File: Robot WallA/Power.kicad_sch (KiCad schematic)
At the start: 25 parts, among them IC6 TLV75533PDBVR, J10 Conn_01x02, J11 Conn_01x02, J12 Conn_01x02, J7 Conn_01x02, J8 XT90PW_M, J9 Conn_01x02

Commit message: Continue to route
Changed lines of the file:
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@@
+	)
+	(label "5V_ACTUATORS"
+		(at 257.81 153.67 180)
+		(effects
+			(font
+				(size 1.27 1.27)
+			)
+			(justify right bottom)
+		)
 	)
 	(label "5V_ACTUATORS"
@@
 		)
 	)
+	(label "12V"
+		(at 257.81 146.05 180)
+		(effects
+			(font
+				(size 1.27 1.27)
+			)
+			(justify right bottom)
+		)
+	)
 	(label "Vbatt"
 		(at 41.91 99.06 0)
@@
 		)
 	)
+	(label "5V_COMPUTE"
+		(at 257.81 149.86 180)
+		(effects
+			(font
+				(size 1.27 1.27)
+			)
+			(justify right bottom)
+		)
+	)
 	(label "5V_ACTUATORS"
 		(at 257.81 128.27 180)
@@
 	(label "3V3"
 		(at 130.81 76.2 180)
+		(effects
+			(font
+				(size 1.27 1.27)
+			)
+			(justify right bottom)
+		)
+	)
+	(label "24V"
+		(at 257.81 142.24 180)
 		(effects
 			(font
@@
 			)
 			(justify left)
+		)
+	)
+	(netclass_flag ""
+		(length 2.54)
+		(shape round)
+		(at 257.81 153.67 270)
+		(effects
+			(font
+				(size 1.27 1.27)
+			)
+			(justify right bottom)
+		)
+		(property "Netclass" "HighCurrent_3A"
+			(at 261.112 153.67 0)
+			(effects
+				(font
+					(size 1.27 1.27)
+				)
+				(justify left)
+			)
+		)
+		(property "Component Class" ""
+			(at -34.29 92.71 0)
+			(effects
+				(font
+					(size 1.27 1.27)
+					(italic yes)
+				)
+			)
+		)
+	)
+	(netclass_flag ""
+		(length 2.54)
+		(shape round)
+		(at 257.81 142.24 270)
+		(effects
+			(font
+				(size 1.27 1.27)
+			)
+			(justify right bottom)
+		)
+		(property "Netclass" "HighCurrent_5A"
+			(at 261.112 142.24 0)
+			(effects
+				(font
+					(size 1.27 1.27)
+				)
+				(justify left)
+			)
+		)
+		(property "Component Class" ""
+			(at -34.29 81.28 0)
+			(effects
+				(font
+					(size 1.27 1.27)
+					(italic yes)
+				)
+			)
+		)
+	)
+	(netclass_flag ""
+		(length 2.54)
+		(shape round)
+		(at 257.81 149.86 270)
+		(effects
+			(font
+				(size 1.27 1.27)
+			)
+			(justify right bottom)
+		)
+		(property "Netclass" "HighCurrent_3A"
+			(at 261.112 149.86 0)
+			(effects
+				(font
+					(size 1.27 1.27)
+				)
+				(justify left)
+			)
+		)
+		(property "Component Class" ""
+			(at -34.29 88.9 0)
+			(effects
+				(font
+					(size 1.27 1.27)
+					(italic yes)
+				)
+			)
+		)
+	)
+	(netclass_flag ""
+		(length 2.54)
+		(shape round)
+		(at 36.83 99.06 180)
+		(effects
+			(font
+				(size 1.27 1.27)
+			)
+			(justify right bottom)
+		)
+		(property "Netclass" "HighCurrent_5A"
+			(at 43.18 103.378 0)
+			(effects
+				(font
+					(size 1.27 1.27)
+				)
+				(justify right)
+			)
+		)
+		(property "Component Class" ""
+			(at 97.79 -193.04 90)
+			(effects
+				(font
+					(size 1.27 1.27)
+					(italic yes)
+				)
+			)
+		)
+	)
+	(netclass_flag ""
+		(length 2.54)
+		(shape round)
+		(at 257.81 146.05 270)
+		(effects
+			(font
+				(size 1.27 1.27)
+			)
+			(justify right bottom)
+		)
+		(property "Netclass" "HighCurrent_5A"
+			(at 261.112 146.05 0)
+			(effects
+				(font
+					(size 1.27 1.27)
+				)
+				(justify left)
+			)
+		)
+		(property "Component Class" ""
+			(at -34.29 85.09 0)
+			(effects
+				(font
+					(size 1.27 1.27)
+					(italic yes)
+				)
+			)
 		)
 	)
@@
 		(on_board yes)
 		(dnp no)
-		(fields_autoplaced yes)
 		(property "Reference" "#PWR049"
 			(at 34.29 100.33 0)
@@
 		)
 		(property "Value" "GND"
-			(at 34.29 99.06 0)
-			(effects
-				(font
+			(at 34.036 97.79 0)
+			(effects
+				(font

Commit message: Updated fab files.
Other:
- company: (none) -> Socotec Monitoring
- title: (none) -> Robot Wall-A
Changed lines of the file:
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@@
 	(generator_version "9.0")
 	(paper "A4")
+	(title_block
+		(title "Robot Wall-A")
+		(date "2025-09-20")
+		(rev "v1.0")
+		(company "Socotec Monitoring")
+		(comment 1 "GDU")
+		(comment 2 "THO")
+	)
 	(text "Cavaliers spécial qui résistent à 5A"
 		(exclude_from_sim no)
@@
 			)
 		)
+		(property "MPN" ""
+			(at 257.81 120.65 90)
+			(effects
+				(font
+					(size 1.27 1.27)
+				)
+				(hide yes)
+			)
+		)
 		(pin "1"
 		)
@@
 			)
 		)
+		(property "MPN" ""
+			(at 118.11 133.35 90)
+			(effects
+				(font
+					(size 1.27 1.27)
+				)
+				(hide yes)
+			)
+		)
 		(pin "1"
 		)
@@
 			)
 		)
+		(property "MPN" ""
+			(at 34.29 88.9 90)
+			(effects
+				(font
+					(size 1.27 1.27)
+				)
+				(hide yes)
+			)
+		)
 		(pin "1"
 		)
@@
 			)
 		)
+		(property "MPN" ""
+			(at 77.47 162.56 0)
+			(effects
+				(font
+					(size 1.27 1.27)
+				)
+				(hide yes)
+			)
+		)
 		(pin "1"
 		)
@@
 			)
 		)
+		(property "MPN" ""
+			(at 257.81 116.84 90)
+			(effects
+				(font
+					(size 1.27 1.27)
+				)
+				(hide yes)
+			)
+		)
 		(pin "1"
 		)
@@
 			)
 		)
+		(property "MPN" ""
+			(at 77.47 172.72 0)
+			(effects
+				(font
+					(size 1.27 1.27)
+				)
+				(hide yes)
+			)
+		)
 		(pin "1"
 		)
@@
 			)
 		)
+		(property "MPN" ""
+			(at 36.83 137.16 0)
+			(effects
+				(font
+					(size 1.27 1.27)
+				)
+				(hide yes)
+			)
+		)
 		(instances
 			(project "Robot WallA"
@@
 			)
 		)
+		(property "MPN" ""
+			(at 262.89 88.9 0)
+			(effects
+				(font
+					(size 1.27 1.27)
+				)
+				(hide yes)
+			)
+		)
 		(pin "1"
 		)
@@
 			)
 		)
+		(property "MPN" ""
+			(at 36.83 128.27 0)
+			(effects
+				(font
+					(size 1.27 1.27)
+				)
+				(hide yes)
+			)
+		)
 		(instances
 			(project "Robot WallA"
@@
 			)
 		)
+		(property "MPN" ""
+			(at 262.89 96.52 0)
+			(effects
+				(font
+					(size 1.27 1.27)
+				)
+				(hide yes)
+			)
+		)
 		(pin "1"
 		)
@@
 			)
 		)
+		(property "MPN" ""
+			(at 127 31.75 90)
+			(effects
+				(font
+					(size 1.27 1.27)
+				)
+				(hide yes)
+			)
+		)
 		(pin "2"
 		)
@@
 			)
 		)
+		(property "MPN" ""
+			(at 116.84 74.93 90)
+			(effects
+				(font
+					(size 1.27 1.27)
+				)
+				(hide yes)
+			)
+		)
 		(pin "1"
 		)
@@
 			)
 		)
+		(property "MPN" ""
+			(at 160.02 179.07 0)
+			(effects
+				(font
+					(size 1.27 1.27)
+				)
+				(hide yes)
+			)
+		)
 		(pin "1"
 		)
@@
 			)
 		)
+		(property "MPN" ""
+			(at 257.81 132.08 90)
+			(effects
+				(font
+					(size 1.27 1.27)
+				)
+				(hide yes)
+			)
+		)
 		(pin "1"
 		)
@@
 			)
 		)
+		(property "MPN" ""
+			(at 118.11 172.72 0)
+			(effects
+				(font
+					(size 1.27 1.27)
+				)
+				(hide yes)
+			)
+		)
 		(pin "5"
 		)
@@
 			)
 		)
+		(property "MPN" ""
+			(at 123.19 109.22 90)
+			(effects
+				(font
+					(size 1.27 1.27)
+				)
+				(hide yes)
+			)
+		)
 		(pin "2"
 		)
@@
 			)
 		)
+		(property "MPN" ""
+			(at 257.81 124.46 90)
+			(effects
+				(font
+					(size 1.27 1.27)
+				)
+				(hide yes)
+			)
+		)
 		(pin "1"
 		)
@@
 			)
 		)
+		(property "MPN" ""
+			(at 148.59 179.07 0)
+			(effects
+				(font
+					(size 1.27 1.27)
+				)
+				(hide yes)
+			)
+		)
 		(pin "1"
 		)
@@
 			)
 		)
+		(property "MPN" ""
+			(at 116.84 104.14 90)
+			(effects
+				(font
+					(size 1.27 1.27)
+				)
+				(hide yes)
+			)
+		)
 		(pin "1"
 		)
@@
 			)
 		)
+		(property "MPN" ""
+			(at 102.87 176.53 0)
+			(effects
+				(font
+					(size 1.27 1.27)
+				)
+				(hide yes)
+			)
+		)
 		(pin "1"
 		)
@@
 			)
 		)
+		(property "MPN" ""
+			(at 257.81 128.27 90)
+			(effects
+				(font
+					(size 1.27 1.27)
+				)
+				(hide yes)
+			)
+		)
 		(pin "1"
 		)
@@
 			)
 		)
+		(property "MPN" ""
+			(at 124.46 138.43 90)
+			(effects
+				(font
+					(size 1.27 1.27)
+				)
+				(hide yes)
+			)
+		)
 		(pin "2"
 		)
@@
 			)
 		)
+		(property "MPN" ""
+			(at 123.19 80.01 90)
+			(effects
+				(font
+					(size 1.27 1.27)
+				)
+				(hide yes)
+			)
+		)
 		(pin "2"
 		)
@@
 			)
 		)
+		(property "MPN" ""
+			(at 93.98 176.53 0)
+			(effects
+				(font
+					(size 1.27 1.27)
+				)
+				(hide yes)
+			)
+		)
 		(pin "1"
 		)
@@
 			(at 36.83 119.38 0)
 			(effects
+				(font
+					(size 1.27 1.27)
+				)
+				(hide yes)
+			)
+		)
+		(property "MPN" ""
+			(at 36.83 119.38 0)
+			(effects

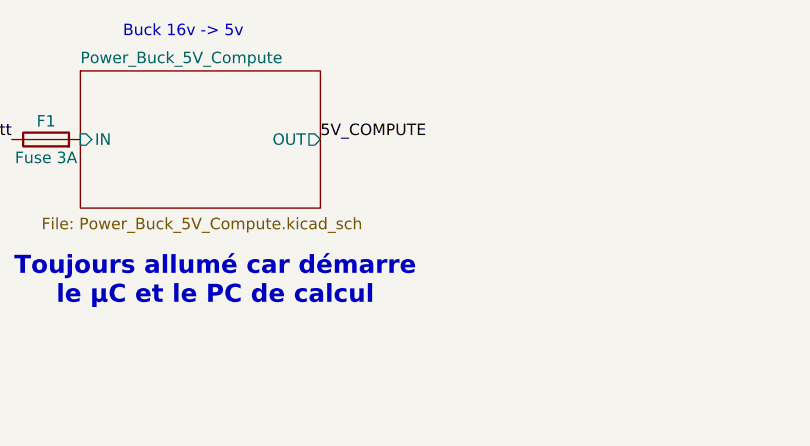
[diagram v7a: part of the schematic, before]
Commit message: Added diode for Type-C connector in case we accidentally power the board with this connector.
Updated fab files
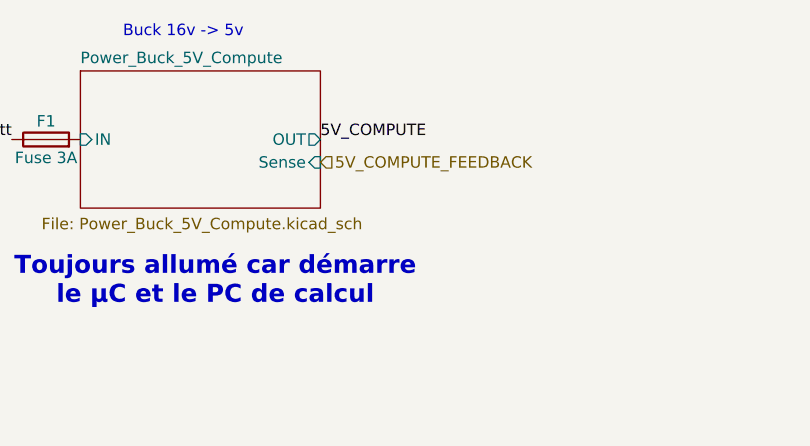
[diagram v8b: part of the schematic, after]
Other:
- sheet Power_Buck_5V_Compute ports: added Sense; removed none
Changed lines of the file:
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@@
+		)
+	)
+	(hierarchical_label "5V_COMPUTE_FEEDBACK"
+		(shape input)
+		(at 157.48 34.29 0)
+		(effects
+			(font
+				(size 1.27 1.27)
+			)
+			(justify left)
 		)
 	)
@@
 			)
 		)
+		(pin "Sense" input
+			(at 157.48 34.29 0)
+			(effects
+				(font
+					(size 1.27 1.27)
+				)
+				(justify right)
+			)
+		)
